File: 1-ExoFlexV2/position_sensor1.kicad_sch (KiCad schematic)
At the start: 24 parts, among them U51 SN74LVC1G08DBVR, U52 SN74LVC1G08DBVR, U53 SN74LVC3G14DCUT_V2

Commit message: Schématisation terminée
- Schéma terminé
- Passage vers le PCB
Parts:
- C43, C44, C45: renamed from C?; value * -> 10nF 10V X5R; footprint Capacitor_SMD:C_0805_2012Metric -> Capacitor_SMD:C_01005_0402Metric; DESCRIPTION (none) -> 10000 pF ±10% 10V Ceramic Capacitor X5R 01005 (0402 Metric); MANUFACTURER (none) -> Murata Electronics; NOTES (none) -> DO NOT POPULATE; PACKAGE (none) -> 01005 (0402 Metric); PART NUMBER (none) -> GRM022R61A103KE19L; TYPE (none) -> SMD
- J100, J101, J102: renamed from J?; value Jmp -> Jumper; footprint (none) -> Connector_PinSocket_2.54mm:PinSocket_1x03_P2.54mm_Vertical; DESCRIPTION (none) -> CONN HEADER VERT 3POS 2.54MM; MANUFACTURER (none) -> Würth Elektronik; PACKAGE (none) -> Square 0.100" (2.54mm); PART NUMBER (none) -> 61300311121; TYPE (none) -> Through Hole
- R137, R138, R139: renamed from R?; DESCRIPTION (none) -> 0 Ohms Jumper Chip Resistor 0805 (2012 Metric) Automotive A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; MANUFACTURER (none) -> Panasonic Electronic Components; PACKAGE (none) -> 0805 (2012 Metric); PART NUMBER (none) -> ERJ-6GEY0R00V; TYPE (none) -> SMD
- R140, R141, R142, R143, R144, R145: renamed from R?; value 100k -> 100k 5% 1/8W; DESCRIPTION (none) -> 100 kOhms ±5% 0.125W, 1/8W Chip Resistor 0805 (2012 Metric)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; MANUFACTURER (none) -> Panasonic Electronic Components; PACKAGE (none) -> 0805 (2012 Metric); PART NUMBER (none) -> ERJ-6GEYJ104V; TYPE (none) -> SMD
- RV27: renamed from RV4; value 1k -> Trim 1k; DESCRIPTION (none) -> Trimmer 1k 0,5W PC PIN TOP; MANUFACTURER (none) -> Bourns Inc.; PACKAGE (none) -> Rectangular - 0.275" x 0.260" Face; PART NUMBER (none) -> 3362P-1-102LF; TYPE (none) -> Through Hole
- RV28: renamed from RV5; value 1k -> Trim 1k; DESCRIPTION (none) -> Trimmer 1k 0,5W PC PIN TOP; MANUFACTURER (none) -> Bourns Inc.; PACKAGE (none) -> Rectangular - 0.275" x 0.260" Face; PART NUMBER (none) -> 3362P-1-102LF; TYPE (none) -> Through Hole
- RV29: renamed from RV6; value 1k -> Trim 1k; DESCRIPTION (none) -> Trimmer 1k 0,5W PC PIN TOP; MANUFACTURER (none) -> Bourns Inc.; PACKAGE (none) -> Rectangular - 0.275" x 0.260" Face; PART NUMBER (none) -> 3362P-1-102LF; TYPE (none) -> Through Hole
- U67, U68, U69: renamed from U?; value LM393DGKR -> COMP; footprint DGK8 -> FootPrint:DGK8; DESCRIPTION (none) -> Comparator General Purpose Open-Collector, Rail-to-Rail 8-V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; MANUFACTURER (none) -> Texas Instruments; PACKAGE (none) -> 8-TSSOP, 8-MSOP (0.118", 3.00mm Width); PART NUMBER (none) -> LM393DGKR; TYPE (none) -> SMD
- U70: renamed from U51; value SN74LVC1G08DBVR -> AND Gate; DESCRIPTION (none) -> AND Gate IC 1 Channel SOT-23-5; MANUFACTURER (none) -> Texas Instruments; PACKAGE (none) -> SC-74A, SOT-753; PART NUMBER (none) -> SN74LVC1G08DBVR; TYPE (none) -> SMD
- U71: renamed from U52; value SN74LVC1G08DBVR -> AND Gate; DESCRIPTION (none) -> AND Gate IC 1 Channel SOT-23-5; MANUFACTURER (none) -> Texas Instruments; PACKAGE (none) -> SC-74A, SOT-753; PART NUMBER (none) -> SN74LVC1G08DBVR; TYPE (none) -> SMD
- U72: renamed from U53; value SN74LVC3G14DCUT_V2 -> Inverter; DESCRIPTION (none) -> Inverter IC 3 Channel Schmitt Trigger 8-VSSOP; MANUFACTURER (none) -> Texas Instruments; PACKAGE (none) -> 8-VFSOP (0.091", 2.30mm Width); PART NUMBER (none) -> SN74LVC3G14DCUT; TYPE (none) -> SMD
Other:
- note added: "3xComp : 5VA @ 77,4mA 2xANDGate : 5V @ 64,02mA 1xNOTGte : 5V @ 32,01mA 3xPot1k : 5VA @ 300mA 6x100k : 5V @ 0,3mA Total current : 5V @ 101mA 5VA @ 382mA"
- note removed: "3xComp : 5VA @ 16,5mA 2xANDGate : 5V @ 64,02mA 1xNOTGte : 5V @ 32,01mA 3xPot1k : 5VA @ 15mA Total current : 5V @ 115mA 5VA @ 16,5mA"
- moved on the sheet: J100, J102, R143, R145

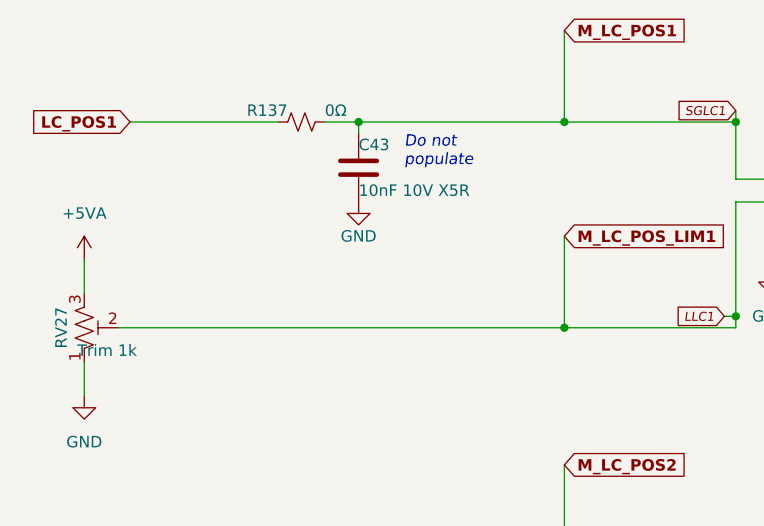
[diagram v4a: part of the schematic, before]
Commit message: Bug NetList
- Ajout de net-tie pour les GND et et les +5V
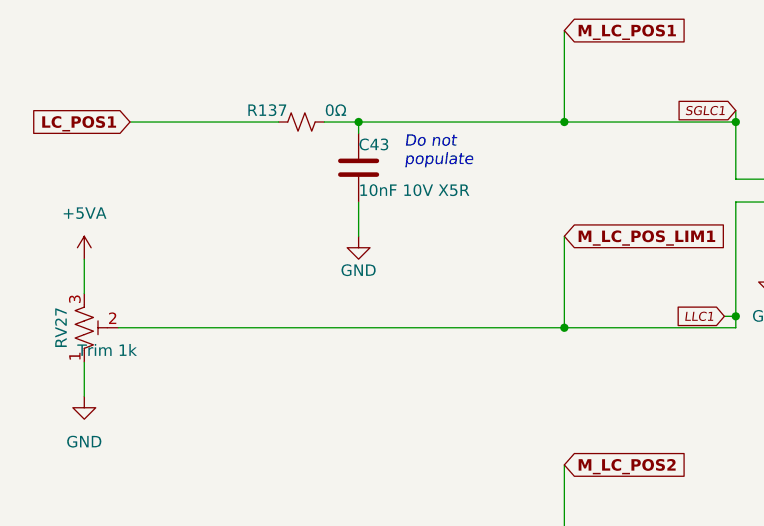
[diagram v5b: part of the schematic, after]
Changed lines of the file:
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@@
+    (stroke (width 0) (type default) (color 0 0 0 0))
+  )
+  (wire (pts (xy 53.34 43.18) (xy 53.34 39.37))
     (stroke (width 0) (type default) (color 0 0 0 0))
   )
@@
   (symbol (lib_id "power:+5VA") (at 119.38 78.74 0) (unit 1)
     (in_bom yes) (on_board yes) (fields_autoplaced)
-    (property "Reference" "#PWR0397" (id 0) (at 119.38 82.55 0)
+    (property "Reference" "#PWR0398" (id 0) (at 119.38 82.55 0)
       (effects (font (size 1.27 1.27)) hide)
     )
@@
   (symbol (lib_id "power:+5VA") (at 22.86 93.98 0) (unit 1)
     (in_bom yes) (on_board yes) (fields_autoplaced)
-    (property "Reference" "#PWR0385" (id 0) (at 22.86 97.79 0)
+    (property "Reference" "#PWR0386" (id 0) (at 22.86 97.79 0)
       (effects (font (size 1.27 1.27)) hide)
     )
@@
   (symbol (lib_id "power:+5V") (at 185.42 127 0) (unit 1)
     (in_bom yes) (on_board yes) (fields_autoplaced)
-    (property "Reference" "#PWR0406" (id 0) (at 185.42 130.81 0)
+    (property "Reference" "#PWR0407" (id 0) (at 185.42 130.81 0)
       (effects (font (size 1.27 1.27)) hide)
     )
@@
   (symbol (lib_id "power:GND") (at 53.34 87.63 0) (unit 1)
     (in_bom yes) (on_board yes)
-    (property "Reference" "#PWR0390" (id 0) (at 53.34 93.98 0)
+    (property "Reference" "#PWR0391" (id 0) (at 53.34 93.98 0)
       (effects (font (size 1.27 1.27)) hide)
     )
@@
   (symbol (lib_id "power:+5VA") (at 22.86 45.72 0) (unit 1)
     (in_bom yes) (on_board yes) (fields_autoplaced)
-    (property "Reference" "#PWR0383" (id 0) (at 22.86 49.53 0)
+    (property "Reference" "#PWR0384" (id 0) (at 22.86 49.53 0)
       (effects (font (size 1.27 1.27)) hide)
     )
@@
   (symbol (lib_id "power:+5VA") (at 119.38 30.48 0) (unit 1)
     (in_bom yes) (on_board yes) (fields_autoplaced)
-    (property "Reference" "#PWR0395" (id 0) (at 119.38 34.29 0)
+    (property "Reference" "#PWR0396" (id 0) (at 119.38 34.29 0)
       (effects (font (size 1.27 1.27)) hide)
     )
@@
   (symbol (lib_id "power:GND") (at 99.06 46.99 0) (unit 1)
     (in_bom yes) (on_board yes) (fields_autoplaced)
-    (property "Reference" "#PWR0392" (id 0) (at 99.06 53.34 0)
+    (property "Reference" "#PWR0393" (id 0) (at 99.06 53.34 0)
       (effects (font (size 1.27 1.27)) hide)
     )
@@
   (symbol (lib_id "power:+5V") (at 198.12 48.26 0) (unit 1)
     (in_bom yes) (on_board yes) (fields_autoplaced)
-    (property "Reference" "#PWR0407" (id 0) (at 198.12 52.07 0)
+    (property "Reference" "#PWR0408" (id 0) (at 198.12 52.07 0)
       (effects (font (size 1.27 1.27)) hide)
     )
@@
   (symbol (lib_id "power:GND") (at 22.86 109.22 0) (unit 1)
     (in_bom yes) (on_board yes) (fields_autoplaced)
-    (property "Reference" "#PWR0386" (id 0) (at 22.86 115.57 0)
+    (property "Reference" "#PWR0387" (id 0) (at 22.86 115.57 0)
       (effects (font (size 1.27 1.27)) hide)
     )
@@
   (symbol (lib_id "power:GND") (at 119.38 95.25 0) (unit 1)
     (in_bom yes) (on_board yes) (fields_autoplaced)
-    (property "Reference" "#PWR0398" (id 0) (at 119.38 101.6 0)
+    (property "Reference" "#PWR0399" (id 0) (at 119.38 101.6 0)
       (effects (font (size 1.27 1.27)) hide)
     )
@@
     (pin "1")
   )
-  (symbol (lib_id "power:GND") (at 53.34 39.37 0) (unit 1)
-    (in_bom yes) (on_board yes)
-    (property "Reference" "#PWR0389" (id 0) (at 53.34 45.72 0)
-      (effects (font (size 1.27 1.27)) hide)
-    )
-    (property "Value" "GND" (id 1) (at 53.34 43.18 0))
-    (property "Footprint" "" (id 2) (at 53.34 39.37 0)
-      (effects (font (size 1.27 1.27)) hide)
-    )
-    (property "Datasheet" "" (id 3) (at 53.34 39.37 0)
+  (symbol (lib_id "power:GND") (at 53.34 43.18 0) (unit 1)
+    (in_bom yes) (on_board yes)
+    (property "Reference" "#PWR0390" (id 0) (at 53.34 49.53 0)
+      (effects (font (size 1.27 1.27)) hide)
+    )
+    (property "Value" "GND" (id 1) (at 53.34 46.99 0))
+    (property "Footprint" "" (id 2) (at 53.34 43.18 0)
+      (effects (font (size 1.27 1.27)) hide)
+    )
+    (property "Datasheet" "" (id 3) (at 53.34 43.18 0)
       (effects (font (size 1.27 1.27)) hide)
     )
@@
   (symbol (lib_id "power:GND") (at 99.06 144.78 0) (unit 1)
     (in_bom yes) (on_board yes) (fields_autoplaced)
-    (property "Reference" "#PWR0394" (id 0) (at 99.06 151.13 0)
+    (property "Reference" "#PWR0395" (id 0) (at 99.06 151.13 0)
       (effects (font (size 1.27 1.27)) hide)
     )
@@
   (symbol (lib_id "power:+5VA") (at 119.38 128.27 0) (unit 1)
     (in_bom yes) (on_board yes) (fields_autoplaced)
-    (property "Reference" "#PWR0399" (id 0) (at 119.38 132.08 0)
+    (property "Reference" "#PWR0400" (id 0) (at 119.38 132.08 0)
       (effects (font (size 1.27 1.27)) hide)
     )
@@
   (symbol (lib_id "power:GND") (at 22.86 60.96 0) (unit 1)
     (in_bom yes) (on_board yes) (fields_autoplaced)
-    (property "Reference" "#PWR0384" (id 0) (at 22.86 67.31 0)
+    (property "Reference" "#PWR0385" (id 0) (at 22.86 67.31 0)
       (effects (font (size 1.27 1.27)) hide)
     )
@@
   (symbol (lib_id "power:GND") (at 255.27 102.87 0) (unit 1)
     (in_bom yes) (on_board yes)
-    (property "Reference" "#PWR0412" (id 0) (at 255.27 109.22 0)
+    (property "Reference" "#PWR0413" (id 0) (at 255.27 109.22 0)
       (effects (font (size 1.27 1.27)) hide)
     )
@@
   (symbol (lib_id "power:+5V") (at 227.33 85.09 0) (unit 1)
     (in_bom yes) (on_board yes)
-    (property "Reference" "#PWR0410" (id 0) (at 227.33 88.9 0)
+    (property "Reference" "#PWR0411" (id 0) (at 227.33 88.9 0)
       (effects (font (size 1.27 1.27)) hide)
     )
@@
   (symbol (lib_id "power:GND") (at 119.38 144.78 0) (unit 1)
     (in_bom yes) (on_board yes) (fields_autoplaced)
-    (property "Reference" "#PWR0400" (id 0) (at 119.38 151.13 0)
+    (property "Reference" "#PWR0401" (id 0) (at 119.38 151.13 0)
       (effects (font (size 1.27 1.27)) hide)
     )
@@
   (symbol (lib_id "power:GND") (at 198.12 69.85 0) (unit 1)
     (in_bom yes) (on_board yes) (fields_autoplaced)
-    (property "Reference" "#PWR0408" (id 0) (at 198.12 76.2 0)
+    (property "Reference" "#PWR0409" (id 0) (at 198.12 76.2 0)
       (effects (font (size 1.27 1.27)) hide)
     )
@@
   (symbol (lib_id "power:GND") (at 53.34 137.16 0) (unit 1)
     (in_bom yes) (on_board yes)
-    (property "Reference" "#PWR0391" (id 0) (at 53.34 143.51 0)
+    (property "Reference" "#PWR0392" (id 0) (at 53.34 143.51 0)
       (effects (font (size 1.27 1.27)) hide)
     )
@@
   (symbol (lib_id "power:GND") (at 22.86 158.75 0) (unit 1)
     (in_bom yes) (on_board yes) (fields_autoplaced)
-    (property "Reference" "#PWR0388" (id 0) (at 22.86 165.1 0)
+    (property "Reference" "#PWR0389" (id 0) (at 22.86 165.1 0)
       (effects (font (size 1.27 1.27)) hide)
     )
@@
   (symbol (lib_id "power:GND") (at 119.38 46.99 0) (unit 1)
     (in_bom yes) (on_board yes) (fields_autoplaced)
-    (property "Reference" "#PWR0396" (id 0) (at 119.38 53.34 0)
+    (property "Reference" "#PWR0397" (id 0) (at 119.38 53.34 0)
       (effects (font (size 1.27 1.27)) hide)
     )
@@
   (symbol (lib_id "power:GND") (at 223.52 102.87 0) (unit 1)
     (in_bom yes) (on_board yes)
-    (property "Reference" "#PWR0409" (id 0) (at 223.52 109.22 0)
+    (property "Reference" "#PWR0410" (id 0) (at 223.52 109.22 0)
       (effects (font (size 1.27 1.27)) hide)
     )
@@
   (symbol (lib_id "power:+5VA") (at 22.86 143.51 0) (unit 1)
     (in_bom yes) (on_board yes) (fields_autoplaced)
-    (property "Reference" "#PWR0387" (id 0) (at 22.86 147.32 0)
+    (property "Reference" "#PWR0388" (id 0) (at 22.86 147.32 0)
       (effects (font (size 1.27 1.27)) hide)
     )
@@
   (symbol (lib_id "power:+5V") (at 156.21 29.21 0) (unit 1)
     (in_bom yes) (on_board yes) (fields_autoplaced)
-    (property "Reference" "#PWR0405" (id 0) (at 156.21 33.02 0)
+    (property "Reference" "#PWR0406" (id 0) (at 156.21 33.02 0)
       (effects (font (size 1.27 1.27)) hide)
     )
@@
   (symbol (lib_id "power:+5V") (at 130.81 128.27 0) (unit 1)
     (in_bom yes) (on_board yes) (fields_autoplaced)
-    (property "Reference" "#PWR0403" (id 0) (at 130.81 132.08 0)
+    (property "Reference" "#PWR0404" (id 0) (at 130.81 132.08 0)
       (effects (font (size 1.27 1.27)) hide)
     )
@@
   (symbol (lib_id "power:+5V") (at 233.68 88.9 0) (unit 1)
     (in_bom yes) (on_board yes) (fields_autoplaced)
-    (property "Reference" "#PWR0411" (id 0) (at 233.68 92.71 0)
+    (property "Reference" "#PWR0412" (id 0) (at 233.68 92.71 0)
       (effects (font (size 1.27 1.27)) hide)
     )
@@
   (symbol (lib_id "power:+5V") (at 152.4 77.47 0) (unit 1)
     (in_bom yes) (on_board yes) (fields_autoplaced)
-    (property "Reference" "#PWR0404" (id 0) (at 152.4 81.28 0)
+    (property "Reference" "#PWR0405" (id 0) (at 152.4 81.28 0)
       (effects (font (size 1.27 1.27)) hide)
     )
@@
   (symbol (lib_id "power:+5V") (at 130.81 78.74 0) (unit 1)
     (in_bom yes) (on_board yes) (fields_autoplaced)
-    (property "Reference" "#PWR0402" (id 0) (at 130.81 82.55 0)
+    (property "Reference" "#PWR0403" (id 0) (at 130.81 82.55 0)
       (effects (font (size 1.27 1.27)) hide)
     )
@@
   (symbol (lib_id "power:+5V") (at 130.81 30.48 0) (unit 1)
     (in_bom yes) (on_board yes) (fields_autoplaced)
-    (property "Reference" "#PWR0401" (id 0) (at 130.81 34.29 0)
+    (property "Reference" "#PWR0402" (id 0) (at 130.81 34.29 0)
       (effects (font (size 1.27 1.27)) hide)
     )
@@
   (symbol (lib_id "power:GND") (at 99.06 95.25 0) (unit 1)
     (in_bom yes) (on_board yes) (fields_autoplaced)
-    (property "Reference" "#PWR0393" (id 0) (at 99.06 101.6 0)
-      (effects (font (size 1.27 1.27)) hide)
-    )
+    (property "Reference" "#PWR0394" (id 0) (at 99.06 101.6 0)
+      (effects (font (size 1.27 1.27)) hide)
+    )
